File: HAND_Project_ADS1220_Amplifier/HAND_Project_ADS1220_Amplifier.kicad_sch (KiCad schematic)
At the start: 16 parts, among them J1 Screw_Terminal_01x04, J2 Conn_01x05_Pin, J7 Conn_01x04_Pin, U1 ADS1220IPWR

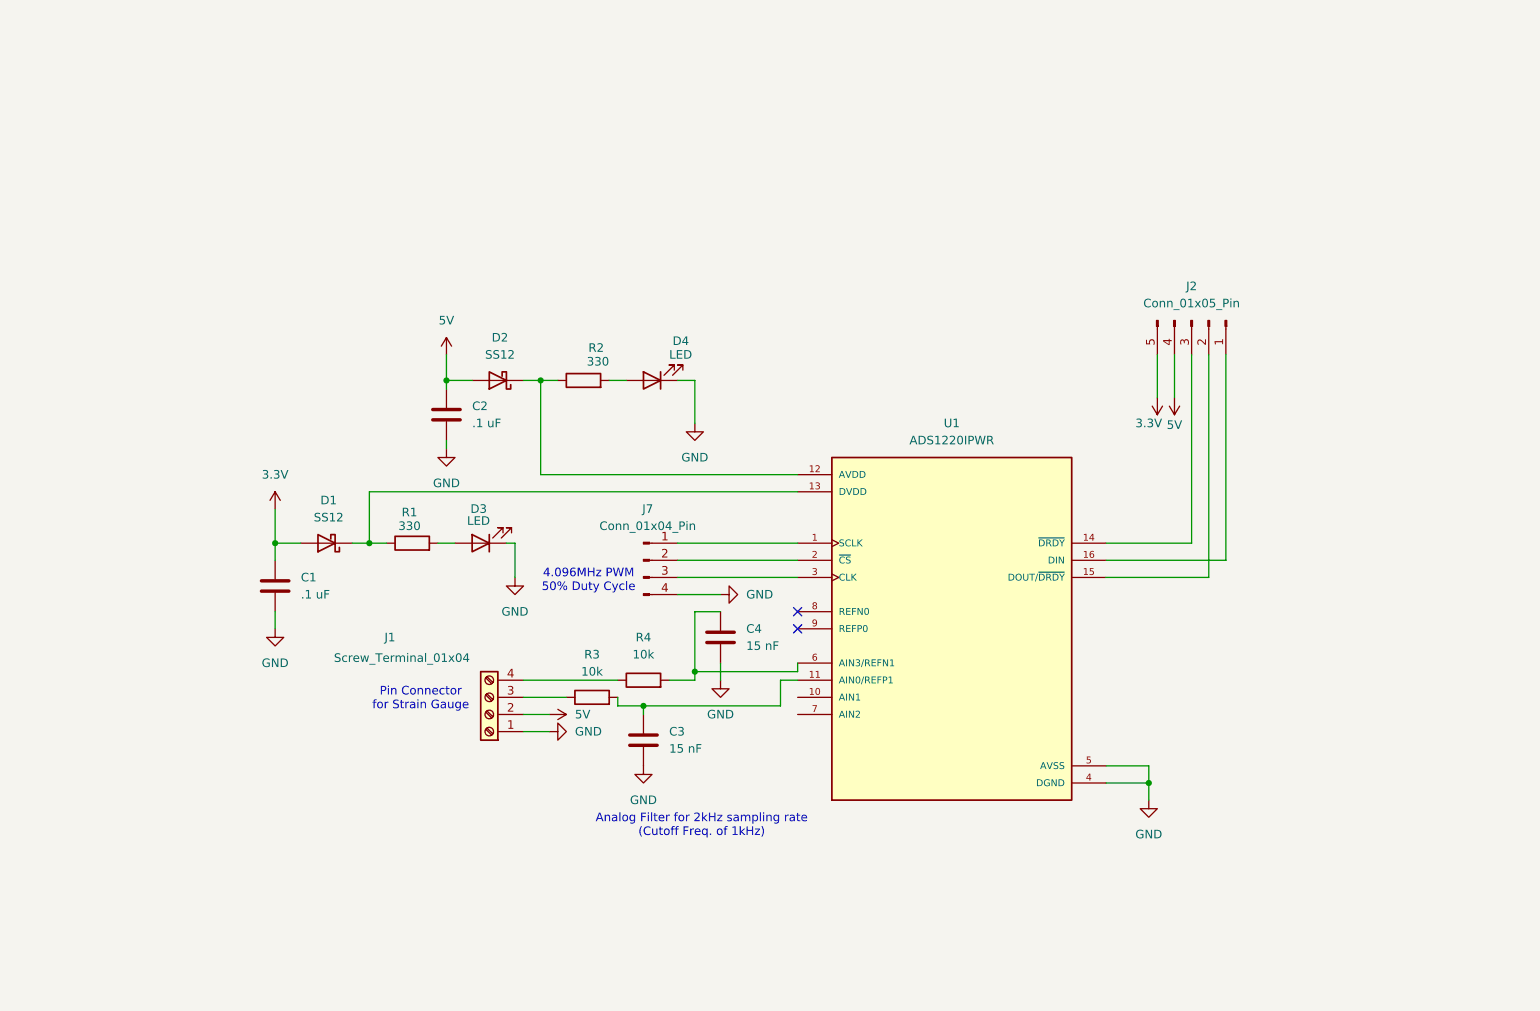
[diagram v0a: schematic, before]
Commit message: Finished Organizing and Sectioning schematic
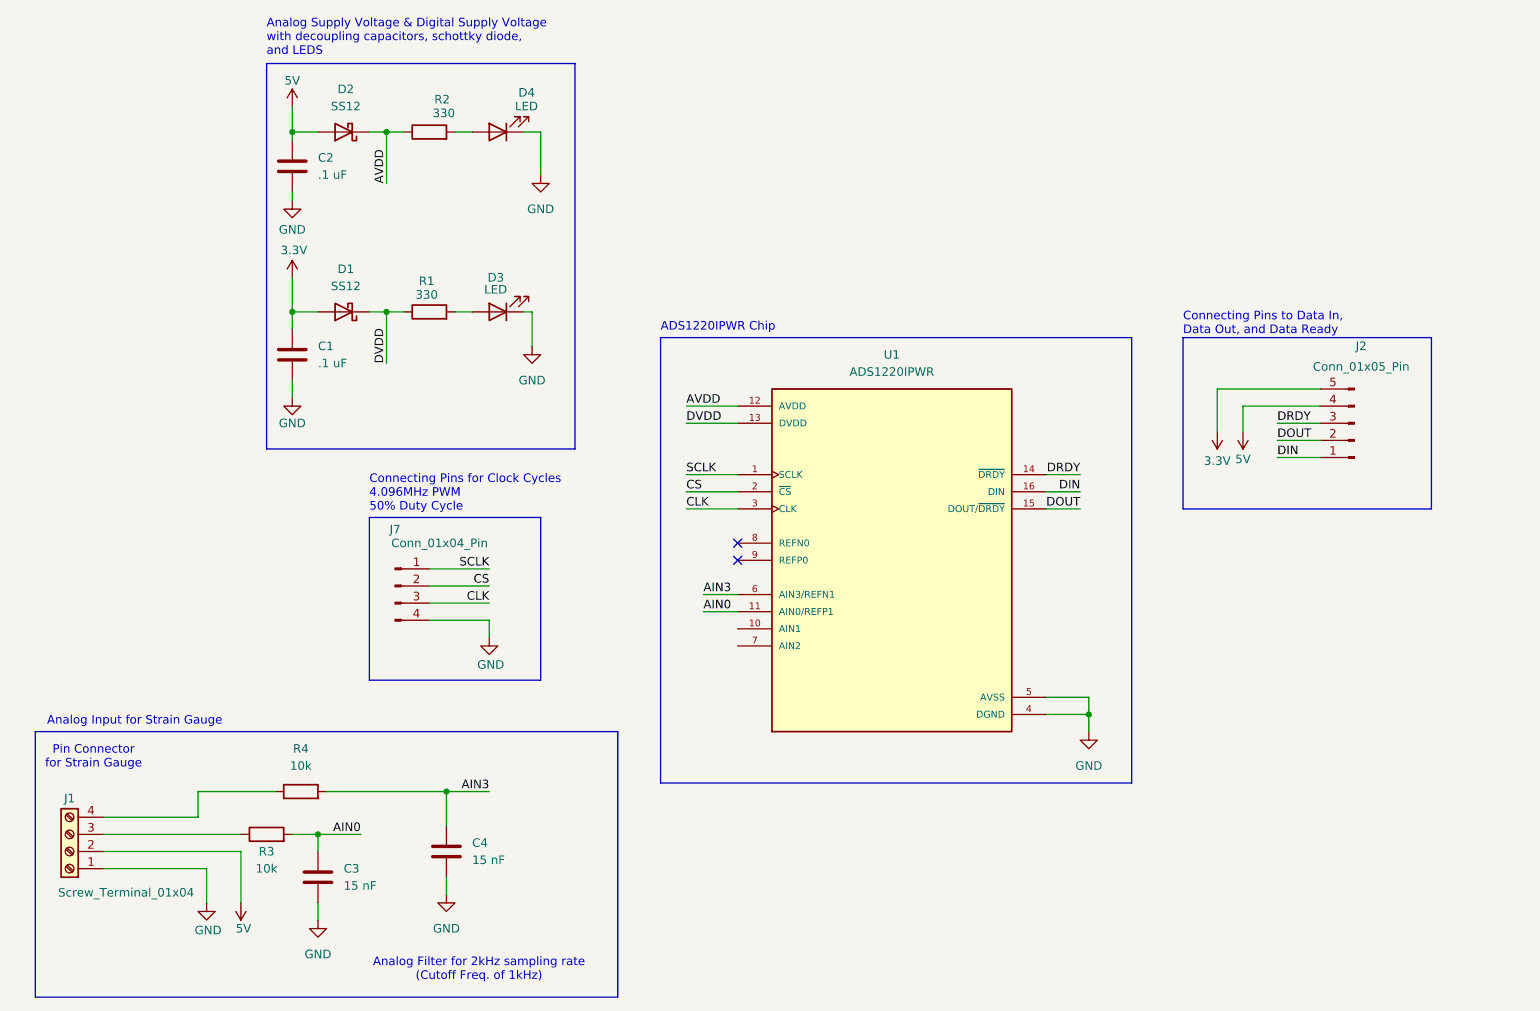
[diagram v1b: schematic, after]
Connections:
- net DVDD: now reaches D1.1 (K), R1.1, U1.13 (DVDD)
- net SCLK: now reaches J7.1 (Pin_1), U1.1 (SCLK)
- net CS: now reaches J7.2 (Pin_2), U1.2 (~{CS})
- net CLK: now reaches J7.3 (Pin_3), U1.3 (CLK)
- net AIN0: now reaches C3.1, R3.2, U1.11 (AIN0/REFP1)
- net DIN: now reaches J2.1 (Pin_1), U1.16 (DIN)
- net DOUT: now reaches J2.2 (Pin_2), U1.15 (DOUT/~{DRDY})
- net DRDY: now reaches J2.3 (Pin_3), U1.14 (~{DRDY})
- net AVDD: now reaches D2.1 (K), R2.1, U1.12 (AVDD)
- net AIN3: now reaches C4.1, R4.2, U1.6 (AIN3/REFN1)
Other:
- note added: "ADS1220IPWR Chip"
- note added: "Analog Input for Strain Gauge"
- note added: "Analog Supply Voltage & Digital Supply Voltage with decoupling capacitors, schottky diode, and LEDS"
- note added: "Connecting Pins for Clock Cycles 4.096MHz PWM 50% Duty Cycle"
- note added: "Connecting Pins to Data In, Data Out, and Data Ready"
- note removed: "4.096MHz PWM 50% Duty Cycle"
- moved on the sheet: C1, C2, C3, C4, D1, D2, D3, D4, J1, J2, J7, R1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

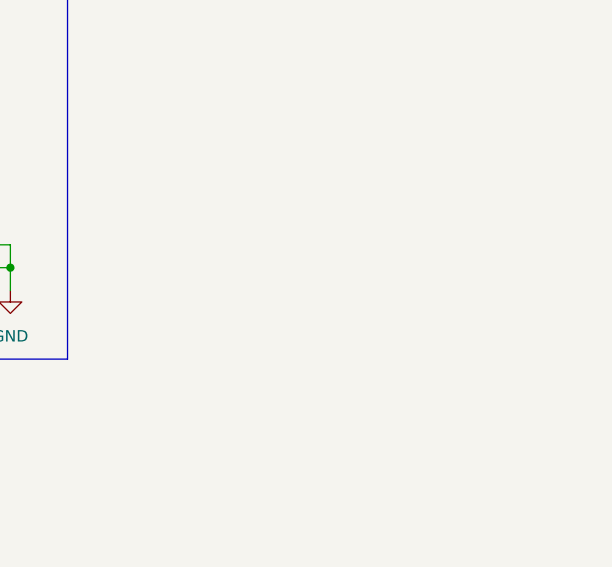
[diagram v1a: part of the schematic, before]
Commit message: Finished Design of PCB without teensy integration
Added external power supply, changed mounting holes to M3, generated gerber files, and the cost to manufacture 3 PCBs is $8.95
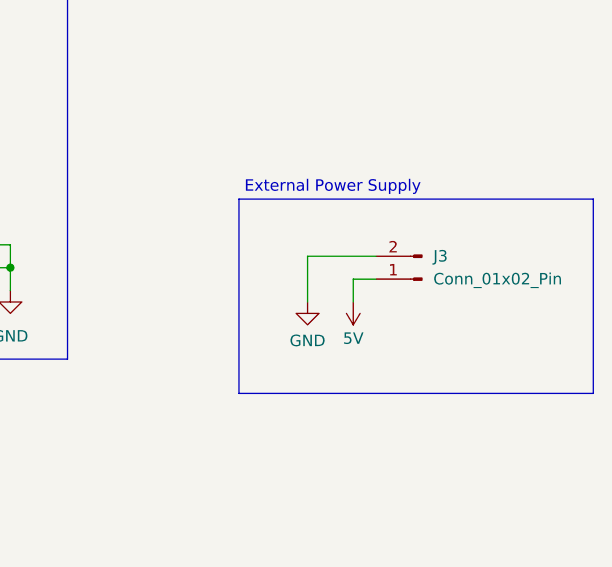
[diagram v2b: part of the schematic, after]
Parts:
- added J3: Conn_01x02_Pin, Connector_JST:JST_PH_B2B-PH-K_1x02_P2.00mm_Vertical, symbol Connector:Conn_01x02_Pin
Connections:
- net 5V: now also J3.1 (Pin_1)
- net GND: now also J3.2 (Pin_2)
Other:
- note added: "External Power Supply"

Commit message: Final touches
matched footprints with yuchan's PCB
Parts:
- removed J3: Conn_01x02_Pin, Connector_JST:JST_PH_B2B-PH-K_1x02_P2.00mm_Vertical, symbol Connector:Conn_01x02_Pin
- C3, C4: value 15 nF -> 10nF
- D3, D4: footprint LED_SMD:LED_0603_1608Metric_Pad1.05x0.95mm_HandSolder -> LED_SMD:LED_0805_2012Metric_Pad1.15x1.40mm_HandSolder
- R1, R2: value 330 -> 360; footprint Resistor_SMD:R_0603_1608Metric_Pad0.98x0.95mm_HandSolder -> Resistor_SMD:R_0805_2012Metric_Pad1.20x1.40mm_HandSolder
- R3, R4: value 10k -> 16k; footprint Resistor_SMD:R_0603_1608Metric_Pad0.98x0.95mm_HandSolder -> Resistor_SMD:R_0805_2012Metric_Pad1.20x1.40mm_HandSolder
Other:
- note removed: "External Power Supply"

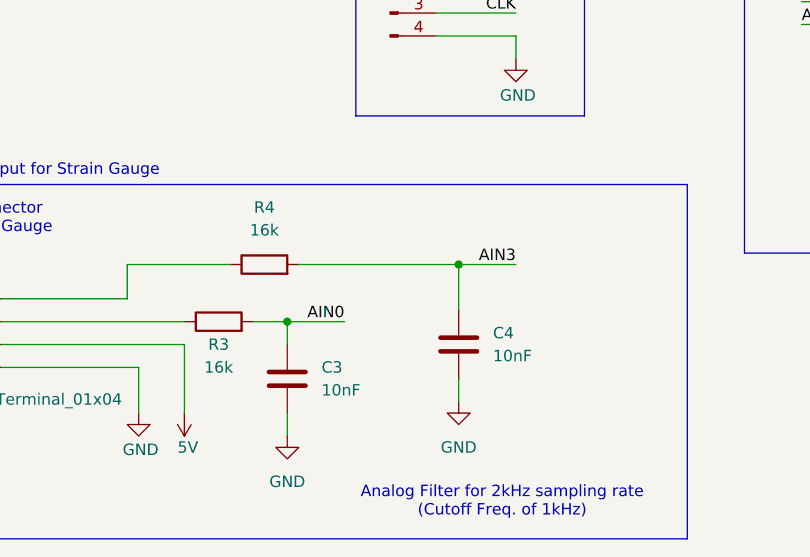
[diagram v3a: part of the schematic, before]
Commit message: new PCB no teensy
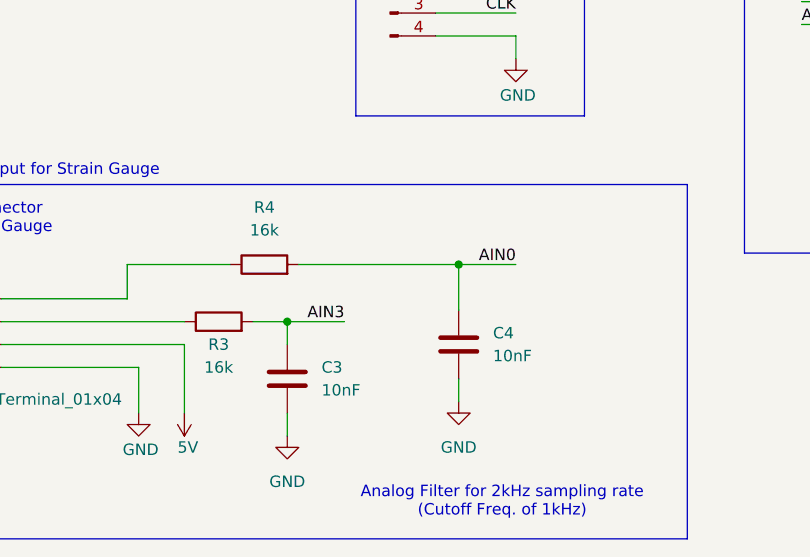
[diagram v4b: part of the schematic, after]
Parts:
- J1: footprint TerminalBlock_Phoenix:TerminalBlock_Phoenix_MKDS-1,5-4_1x04_P5.00mm_Horizontal -> TerminalBlock_Phoenix:TerminalBlock_Phoenix_MPT-0,5-4-2.54_1x04_P2.54mm_Horizontal
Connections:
- net AIN0: now also C4.1, R4.2; no longer C3.1, R3.2
- net AIN3: now also C3.1, R3.2; no longer C4.1, R4.2
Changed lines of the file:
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@@
 		)
 	)
-	(label "AIN0"
+	(label "AIN3"
 		(at 68.58 139.7 180)
 		(effects
@@
 		)
 	)
-	(label "AIN3"
+	(label "AIN0"
 		(at 87.63 133.35 180)
 		(effects
@@
 			)
 		)
-		(property "Footprint" "TerminalBlock_Phoenix:TerminalBlock_Phoenix_MKDS-1,5-4_1x04_P5.00mm_Horizontal"
+		(property "Footprint" "TerminalBlock_Phoenix:TerminalBlock_Phoenix_MPT-0,5-4-2.54_1x04_P2.54mm_Horizontal"
 			(at 25.4 142.24 0)
 			(effects
